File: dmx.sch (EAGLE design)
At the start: 17 parts, among them IC7 FT232RL, IC8 MAX487, X7 USB-SMD-NS

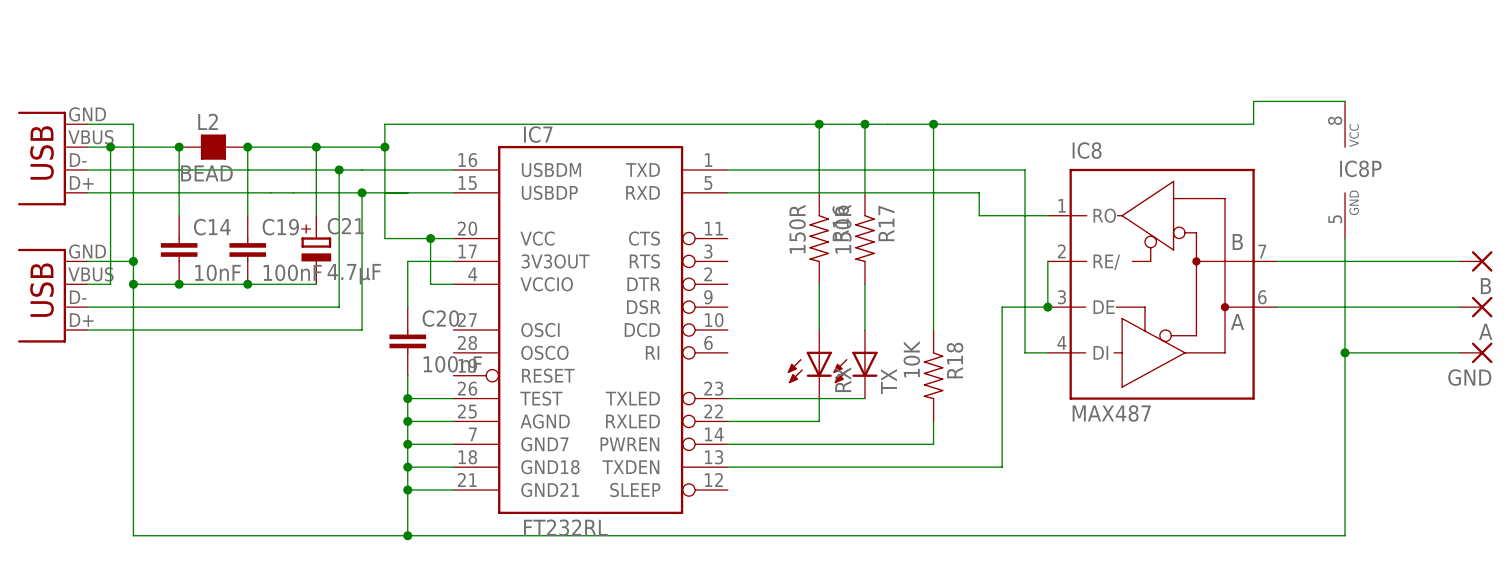
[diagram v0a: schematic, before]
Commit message: proper termination
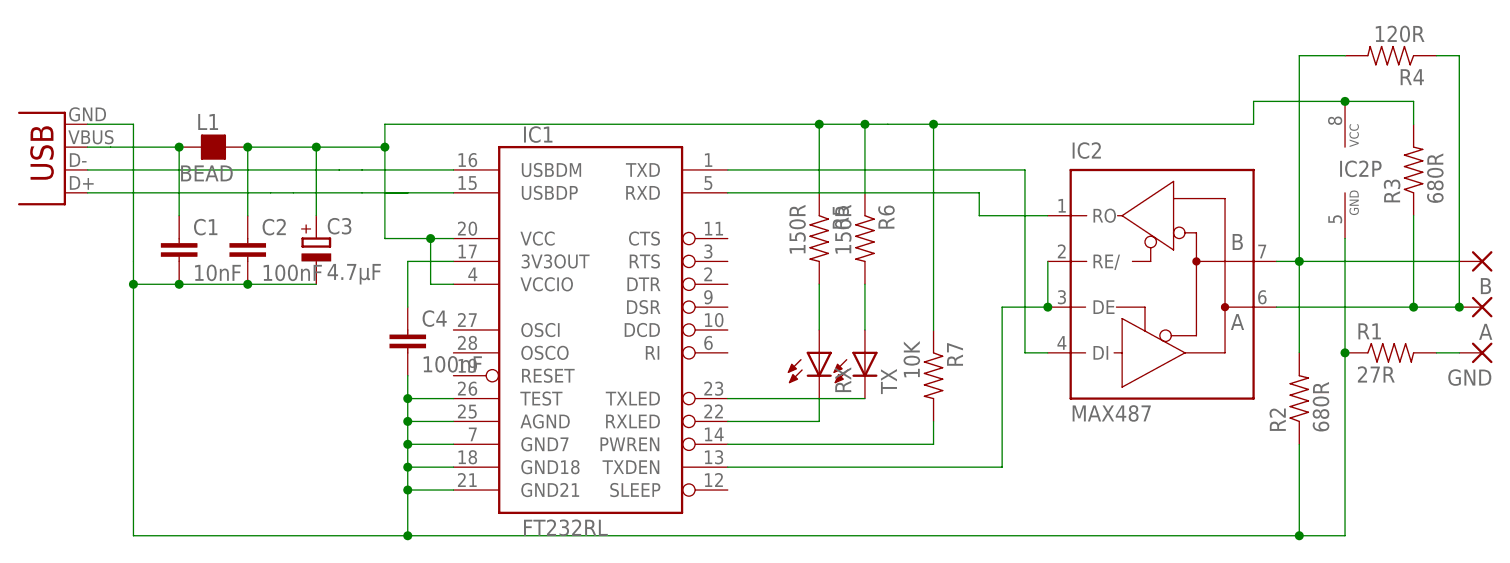
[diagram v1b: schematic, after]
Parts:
- removed JP1: USB-B, SparkFun-Connectors:USBPTH
- added R1: 27R, SparkFun:RESISTOR0805-RES
- added R2, R3: 680R, SparkFun:RESISTOR0805-RES
- added R4: 120R, SparkFun:RESISTOR0805-RES
- renumbered C14 to C1, C19 to C2, C20 to C4, C21 to C3, IC7 to IC1, IC8 to IC2, L2 to L1, R16 to R5, R17 to R6, R18 to R7
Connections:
- new net N$2: GND.P, R1.2
- net +USB_SIEVED: now also R3.2
- net GND_USB: now also R1.1, R2.1; no longer GND.P, JP1.GND
- net N$24: no longer JP1.D+
- net N$30: no longer JP1.VBUS
- net N$5: now also R2.2, R4.2
- net N$6: now also R3.1, R4.1
- net N$7: no longer JP1.D-
